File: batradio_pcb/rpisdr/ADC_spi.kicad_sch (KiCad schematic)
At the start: 21 parts, among them U2 mcp33131, U3 ldln025

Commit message: Update rpi_adc_stream
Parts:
- U4: value (none) -> ths4521; footprint (none) -> Package_SO:VSSOP-8_3.0x3.0mm_P0.65mm
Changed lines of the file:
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@@
     (in_bom yes) (on_board yes)
     (property "Reference" "U4" (id 0) (at 85.09 64.77 0))
-    (property "Value" "" (id 1) (at 89.3572 100.6602 0))
-    (property "Footprint" "" (id 2) (at 88.9 80.01 0)
+    (property "Value" "ths4521" (id 1) (at 89.3572 100.6602 0))
+    (property "Footprint" "Package_SO:VSSOP-8_3.0x3.0mm_P0.65mm" (id 2) (at 88.9 80.01 0)
       (effects (font (size 1.27 1.27)) hide)
     )

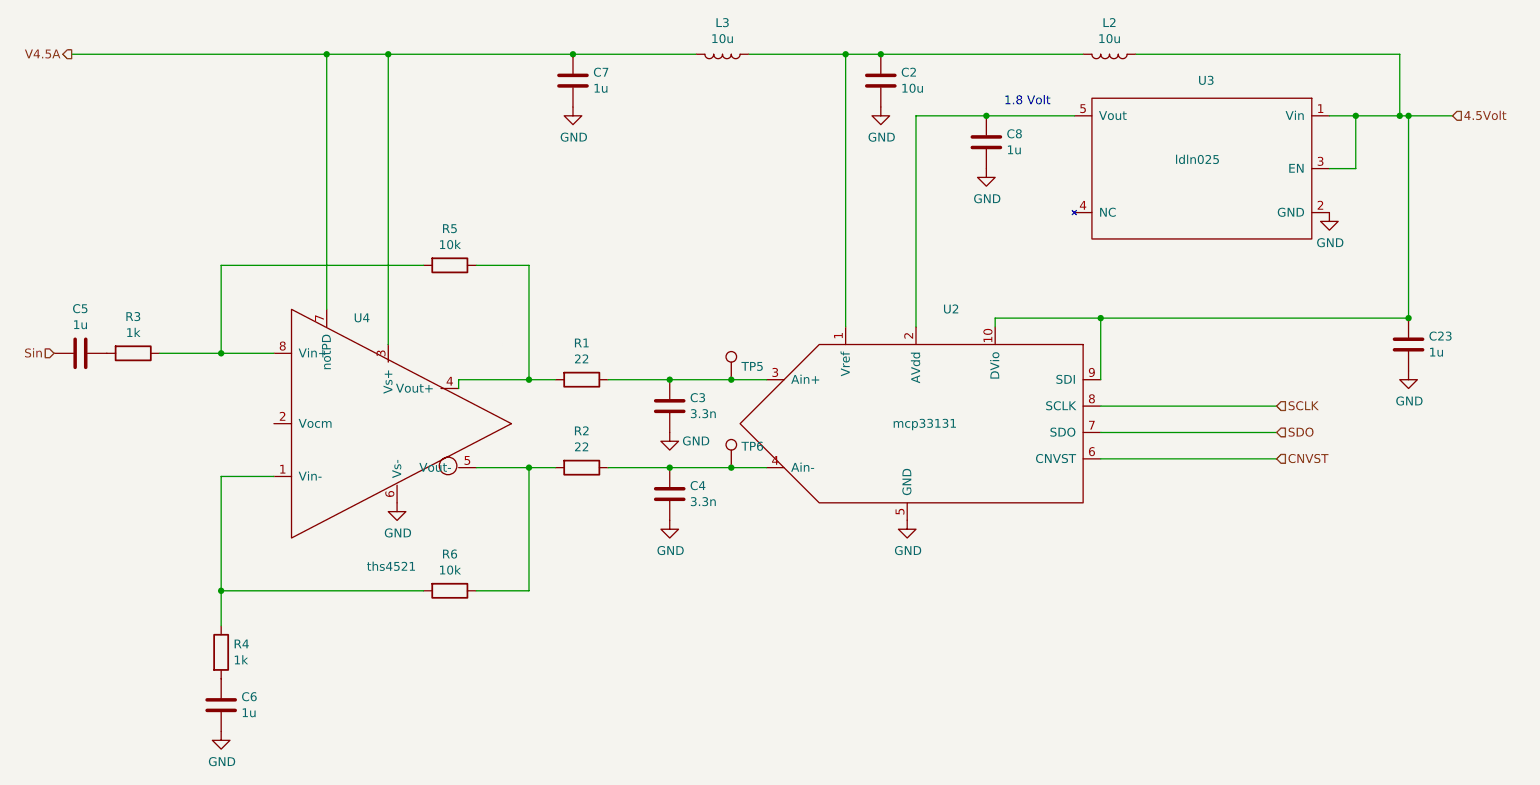
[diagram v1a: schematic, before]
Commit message: Corrected schematic and added mykicadlibs
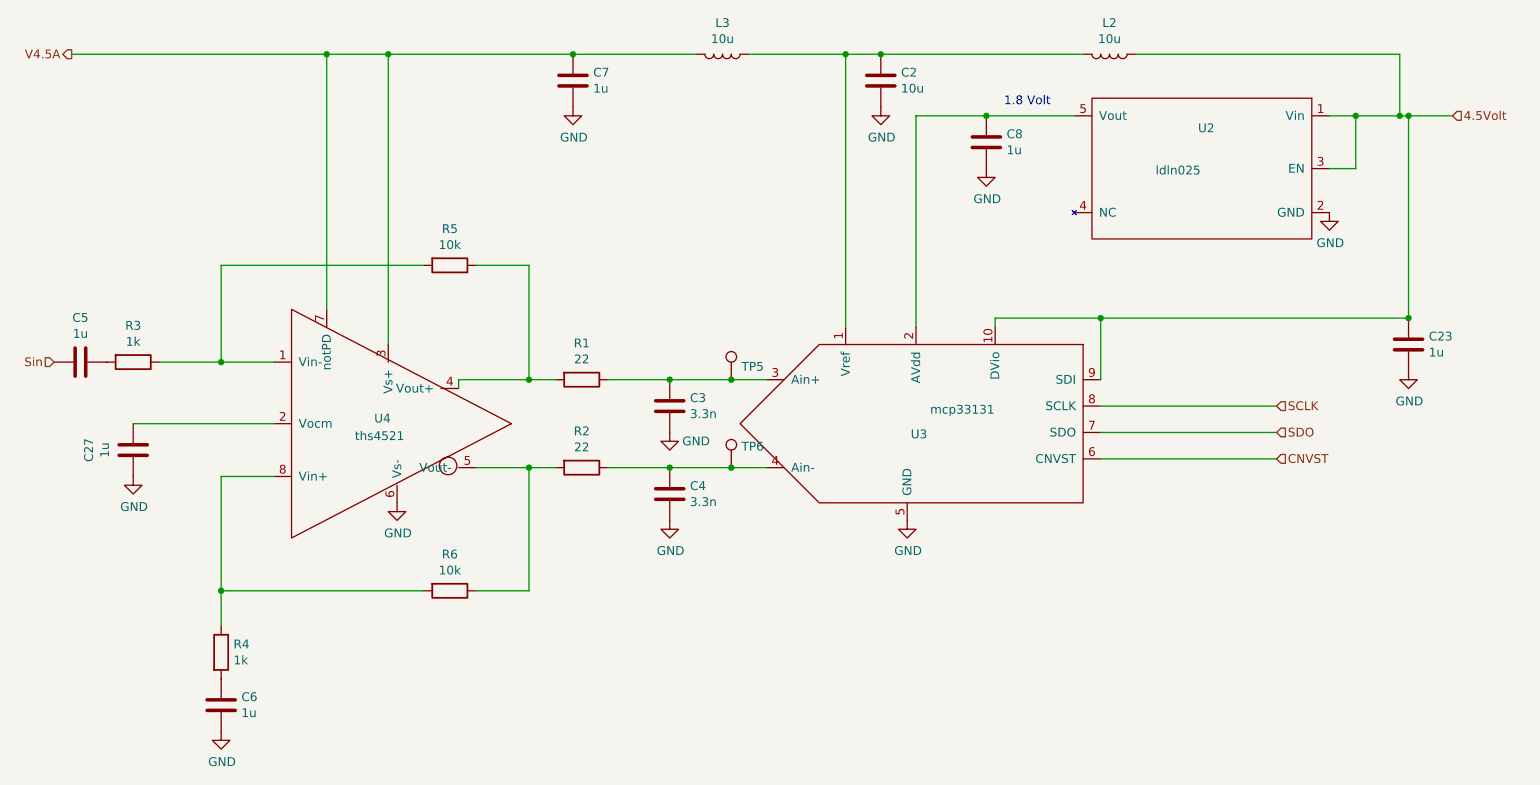
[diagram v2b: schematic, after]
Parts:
- removed U2: mcp33131, Package_SO:MSOP-10_3x3mm_P0.5mm, symbol rpisdr-rescue:mcp33131-mylib
- removed U3: ldln025, Package_TO_SOT_SMD:SOT-23-5, symbol rpisdr-rescue:ldln025-mylib
- removed U4: ths4521, Package_SO:VSSOP-8_3.0x3.0mm_P0.65mm, symbol rpisdr-rescue:ths4521-mylib
- added C27: 1u, Capacitor_SMD:C_1206_3216Metric_Pad1.33x1.80mm_HandSolder, symbol Device:C
- added U2: ldln025, Package_TO_SOT_SMD:SOT-23-5, symbol mylibxx:ldln025
- added U3: mcp33131, library:MSOP-10_3x3mm_P0.5mm, symbol mylibxx:mcp33131
- added U4: ths4521, library:VSSOP-8_3x3mm_P0.65mm, symbol mylibxx:ths4521
- C23, C5, C6, C7, C8: footprint Capacitor_SMD:C_1206_3216Metric_Pad1.42x1.75mm_HandSolder -> Capacitor_SMD:C_1206_3216Metric_Pad1.33x1.80mm_HandSolder
- C3, C4: footprint Capacitor_SMD:C_0805_2012Metric_Pad1.15x1.40mm_HandSolder -> Capacitor_SMD:C_0805_2012Metric_Pad1.18x1.45mm_HandSolder
- R1, R2, R3, R4, R5, R6: footprint Resistor_SMD:R_0805_2012Metric_Pad1.15x1.40mm_HandSolder -> Resistor_SMD:R_0805_2012Metric_Pad1.20x1.40mm_HandSolder
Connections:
- net 4.5Volt: now also U2.1 (Vin), U2.3 (EN), U3.10 (DVio), U3.9 (SDI)
- net CNVST: now also U3.6 (CNVST)
- net GND: now also C27.2, U2.2 (GND), U3.5 (GND), U4.6 (Vs-)
- net SCLK: now also U3.8 (SCLK)
- net SDO: now also U3.7 (SDO)
- net V4.5A: now also U4.3 (Vs+), U4.7 (notPD)
- net at C2.1, L2.2, L3.1: now also U3.1 (Vref)
- net at C8.1: now also U2.5 (Vout), U3.2 (AVdd)
- net at C3.1, R1.1, TP5.1: now also U3.3 (Ain+)
- net at C4.1, R2.1, TP6.1: now also U3.4 (Ain-)
- net at R4.1, R6.2: now also U4.8 (Vin+)
- net at R1.2, R5.1: now also U4.4 (Vout+)
- net at R2.2, R6.1: now also U4.5 (Vout-)
- net at R3.1, R5.2: now also U4.1 (Vin-)
- new net: C27.1, U4.2 (Vocm)
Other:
- moved on the sheet: C5, R3

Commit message: Corrected mylib library settings
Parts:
- U2: symbol mylibxx:ldln025 -> mylib:ldln025
- U3: symbol mylibxx:mcp33131 -> mylib:mcp33131
- U4: symbol mylibxx:ths4521 -> mylib:ths4521
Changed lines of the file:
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@@
 	)
 	(symbol
-		(lib_id "mylibxx:ths4521")
+		(lib_id "mylib:ths4521")
 		(at 88.9 80.01 0)
 		(unit 1)
@@
 	)
 	(symbol
-		(lib_id "mylibxx:ldln025")
+		(lib_id "mylib:ldln025")
 		(at 209.55 40.64 0)
 		(mirror y)
@@
 	)
 	(symbol
-		(lib_id "mylibxx:mcp33131")
+		(lib_id "mylib:mcp33131")
 		(at 173.99 80.01 0)
 		(unit 1)
